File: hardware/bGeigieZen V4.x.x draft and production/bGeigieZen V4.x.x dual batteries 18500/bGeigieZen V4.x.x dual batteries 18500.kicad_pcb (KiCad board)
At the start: 2 copper layers, 129.4 x 64.6 mm, 16 parts, among them J1 M5 2x15 pin, J11 QI input +5V, J2 Geiger IRover, J3 GPS, J4 Geiger Safepulse, J5 Extra support header, J6 Grove, J7 QI GND out, J8 QI input GND, J9 QI battery out

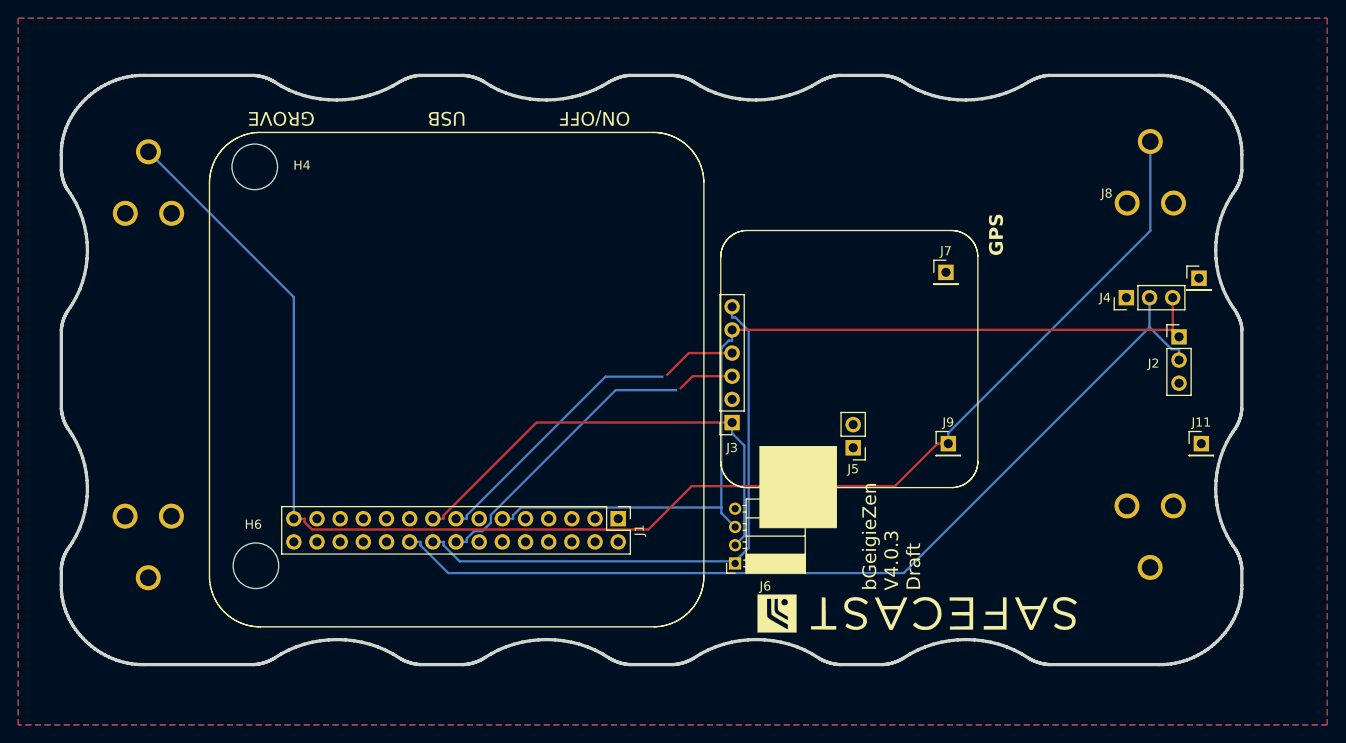
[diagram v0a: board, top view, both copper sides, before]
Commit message: Updated dual 18500 V4.x.x boards
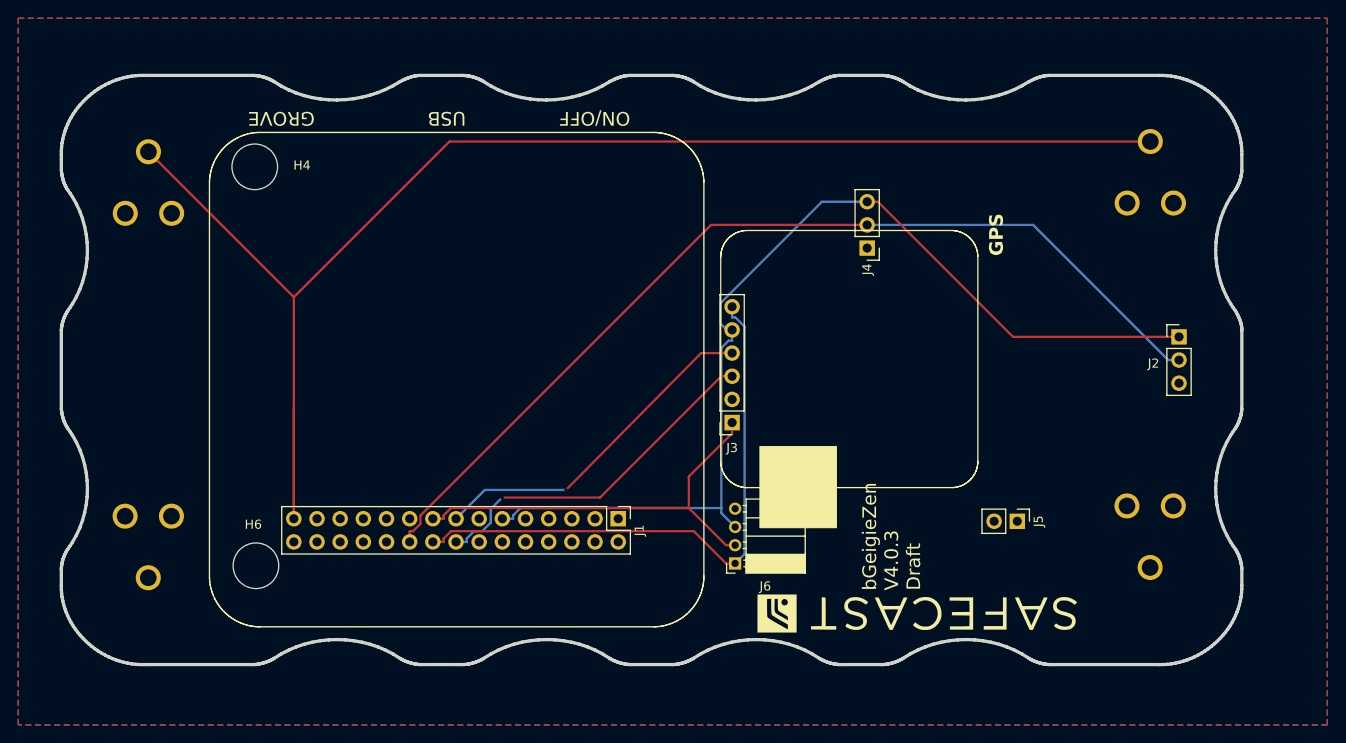
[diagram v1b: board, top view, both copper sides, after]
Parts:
- removed J11: QI input +5V, Connector_PinHeader_2.54mm:PinHeader_1x01_P2.54mm_Vertical
- removed J7: QI GND out, Connector_PinHeader_2.54mm:PinHeader_1x01_P2.54mm_Vertical
- removed J8: QI input GND, Connector_PinHeader_2.54mm:PinHeader_1x01_P2.54mm_Vertical
- removed J9: QI battery out, Connector_PinHeader_2.54mm:PinHeader_1x01_P2.54mm_Vertical
- moved J4 28.9 mm to (172.9, 85.6), turned to 180 degrees
- moved J5 19.7 mm to (189.4, 115.5), turned to -90 degrees
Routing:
- net 3.3V: track 100.5 -> 112.7 mm
- net /BAT: track 165.5 -> 159.9 mm
- net /SDA: track 51.8 -> 46.9 mm
- net /GIO2 on Core and GIO32 on Core-2: track 102.5 -> 106.7 mm
- net /SCL: track 64.0 -> 65.4 mm

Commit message: Changed some layout rerouted traces
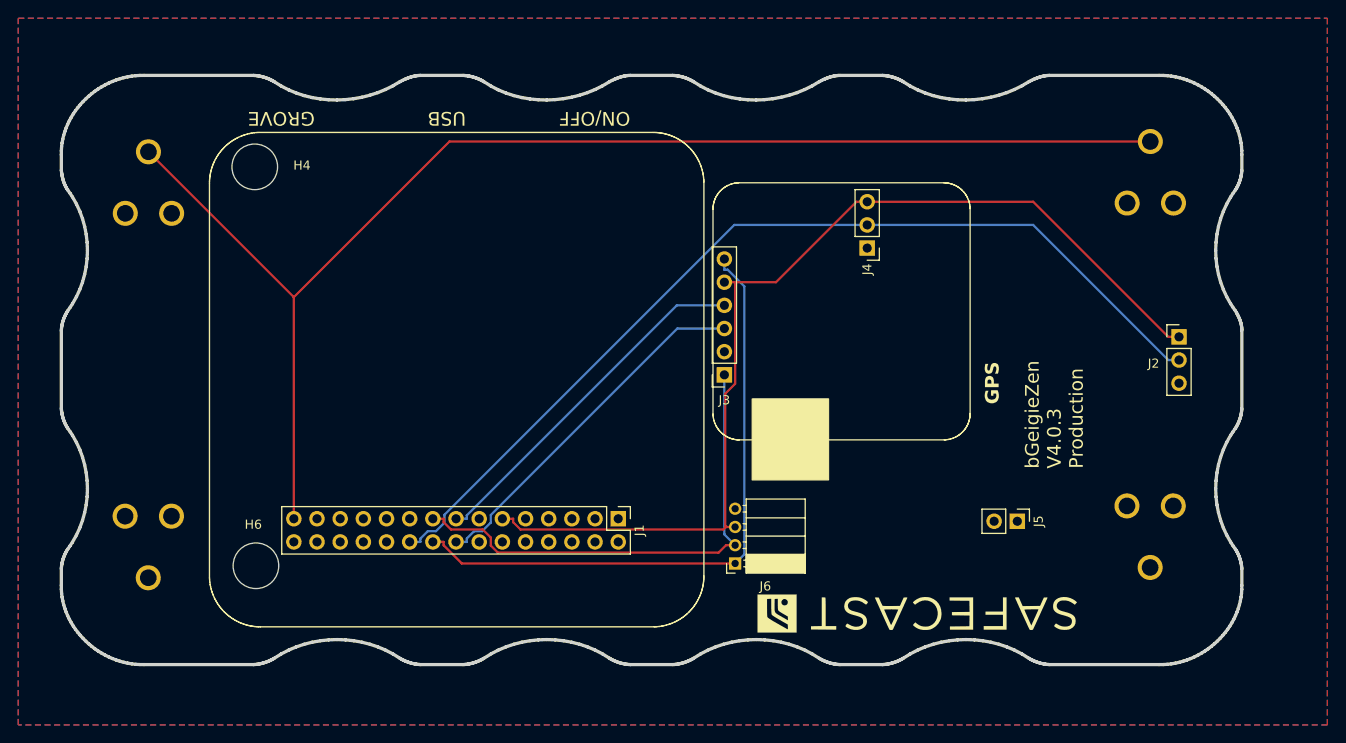
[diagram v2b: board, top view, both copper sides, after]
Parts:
- moved G back 17.7 mm to (176.1, 72.3), turned to 0 degrees
- moved J3 5.30 mm to (157.3, 99.5)
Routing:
- net /BAT: track 159.9 -> 147.8 mm
- net /SDA: track 46.9 -> 54.9 mm
- net /SCL: track 65.4 -> 69.2 mm
- net /RX2: track 37.8 -> 39.3 mm, vias 1 -> 0
- net /GIO2 on Core and GIO32 on Core-2: track 106.7 -> 105.6 mm
- net /TX2: track 38.9 -> 39.8 mm, vias 1 -> 0
- net 3.3V: track 112.7 -> 113.3 mm
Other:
- board text added: "bGeigieZen V4.0.3 Production"
- board text removed: "bGeigieZen V4.0.3 Draft"
